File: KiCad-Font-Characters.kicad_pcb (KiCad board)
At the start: 2 copper layers, 453 x 498 mm, 0 parts

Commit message: Formatting (bold headers, bottom-line)
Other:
- board size 453 x 498 mm -> 453 x 501 mm
- board text added: "${COMPANY} - ${ISSUE_DATE}"
- board text added: "Arrows"
- board text added: "Basic Latin"
- board text added: "Currency Symbols"
- board text added: "Cyrillic Supplement"
- board text added: "General Punctuation"
- board text added: "Greek Extended"
- board text added: "Greek and Coptic"
- board text added: "Halfwidth and Fullwidth Forms"
- board text added: "IPA Extensions"
- board text added: "Latin Extended-B"
- board text added: "Latin1 Supplement"
- board text added: "Mathematical Operators"
- board text added: "Phonetic Extensions"
- board text added: "Superscripts and Subscripts"

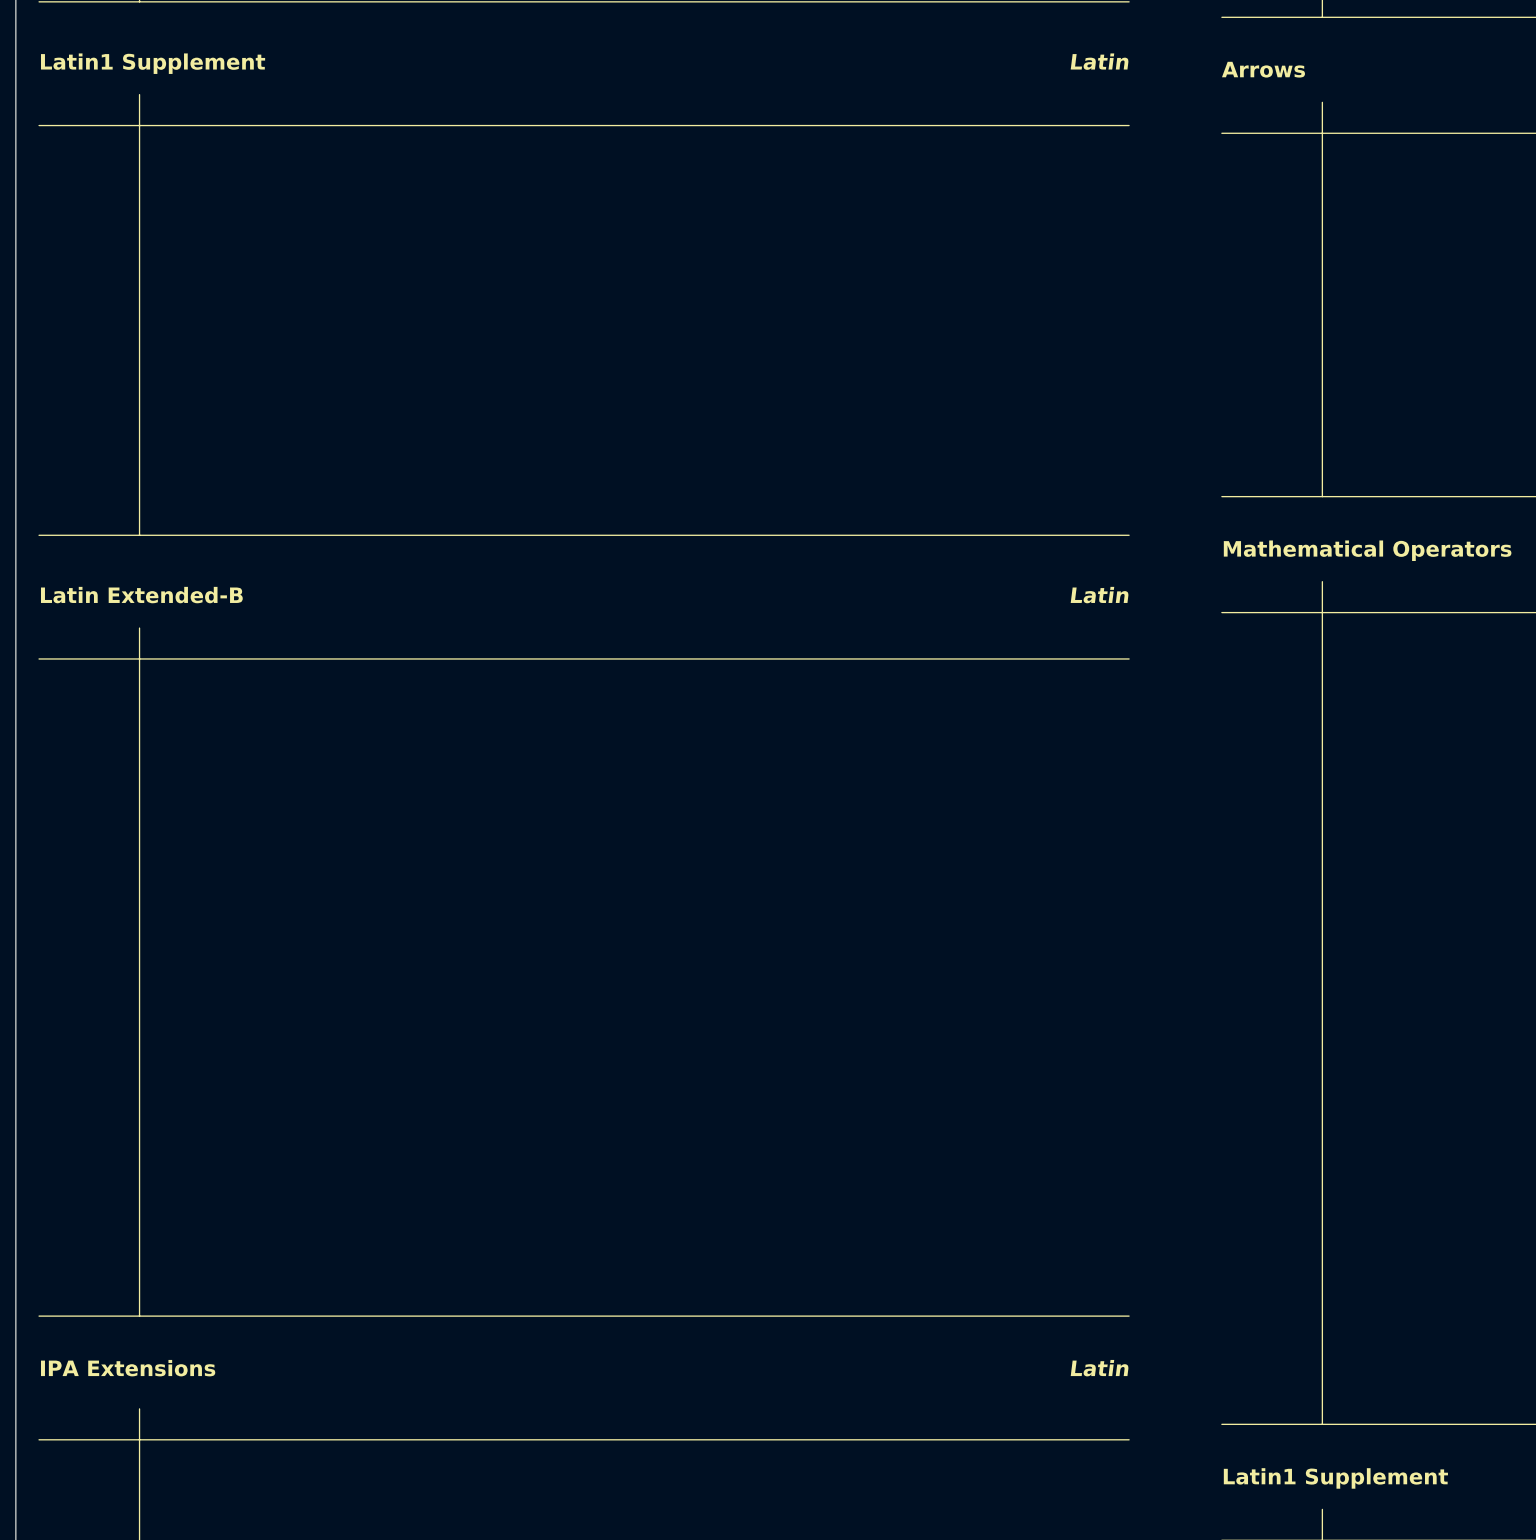
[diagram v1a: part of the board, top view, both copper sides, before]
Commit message: Fixed wrong block names
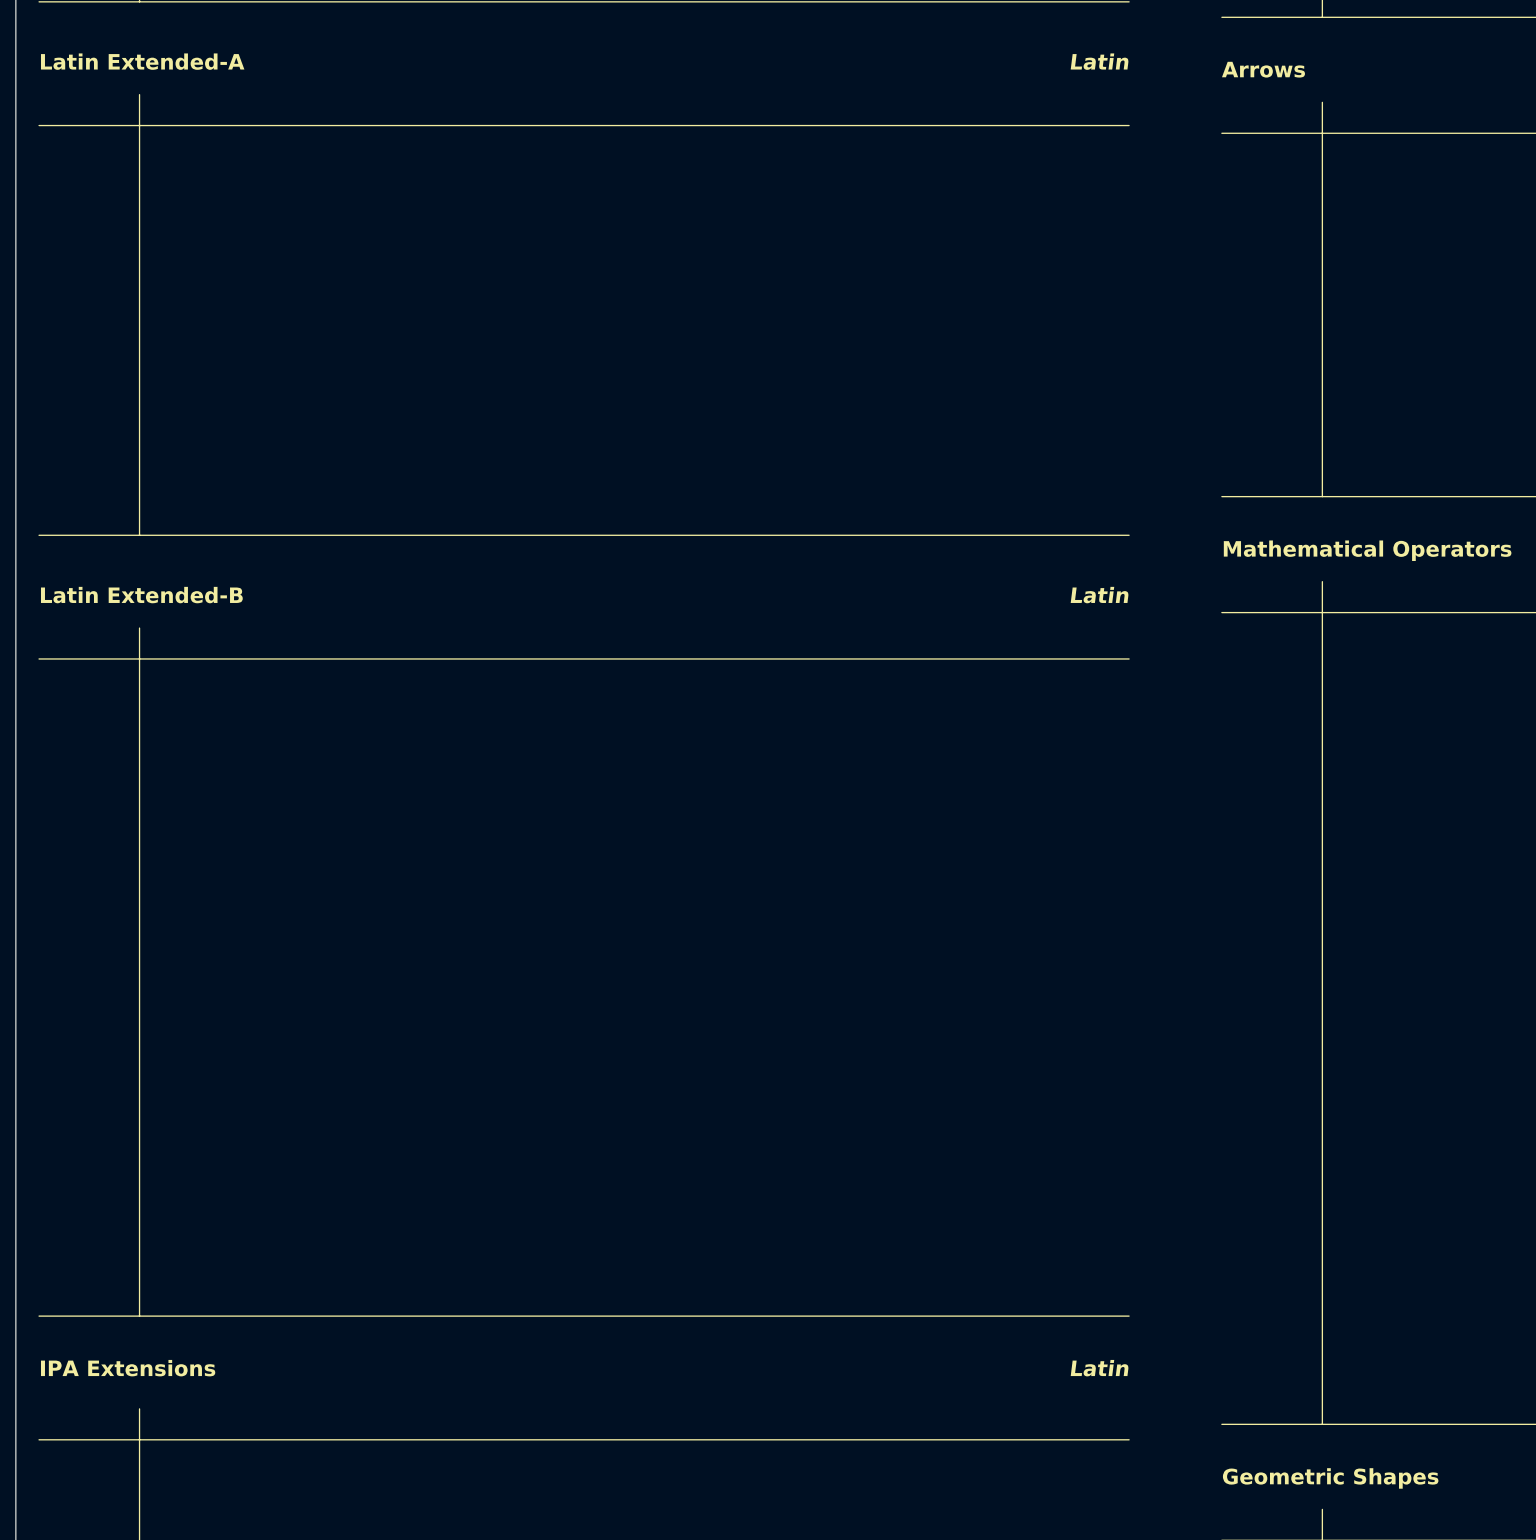
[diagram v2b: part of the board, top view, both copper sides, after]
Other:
- board text added: "Geometric Shapes"
- board text added: "Latin Extended-A"
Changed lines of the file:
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@@
       (sketchpadsonfab false)
       (subtractmaskfromsilk false)
-      (outputformat 5)
+      (outputformat 4)
       (mirror false)
       (drillshape 0)
@@
     (effects (font (size 2 2) (thickness 0.4) bold italic) (justify right bottom))
   )
-  (gr_text "Latin1 Supplement" (at 3 133) (layer "F.SilkS")
+  (gr_text "Latin Extended-A" (at 3 133) (layer "F.SilkS")
     (effects (font (size 2 2) (thickness 0.4) bold) (justify left bottom))
   )
@@
     (effects (font (size 2 2) (thickness 0.4) bold italic) (justify right bottom))
   )
-  (gr_text "Latin1 Supplement" (at 156 316) (layer "F.SilkS")
+  (gr_text "Geometric Shapes" (at 156 316) (layer "F.SilkS")
     (effects (font (size 2 2) (thickness 0.4) bold) (justify left bottom))
   )

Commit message: Fixed annotations
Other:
- board text added: "Grouped by Script. Unimplemented blocks are omitted. ${COMPANY} - ${ISSUE_DATE}"
- board text removed: "${COMPANY} - ${ISSUE_DATE}"
- board text removed: "Unimplemented Blocks are omitted Grouped by Writing System (Script)"
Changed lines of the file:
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@@
     (effects (font (size 2 2) (thickness 0.4) bold italic) (justify right bottom))
   )
-  (gr_text "${COMPANY} - ${ISSUE_DATE}" (at 450 499.117499) (layer "F.SilkS")
+  (gr_text "Grouped by Script.\n\nUnimplemented blocks are omitted.\n\n${COMPANY} - ${ISSUE_DATE}" (at 450 499.117499) (layer "F.SilkS")
     (effects (font (size 2 2) (thickness 0.3)) (justify right bottom))
-  )
-  (gr_text "Unimplemented Blocks are omitted\nGrouped by Writing System (Script)" (at 450 2) (layer "F.SilkS")
-    (effects (font (size 3 3) (thickness 0.375) italic) (justify right top))
   )
   (gr_text "Latin Extended-B" (at 3 202) (layer "F.SilkS")
@@
   (group "" (id 77080d20-7dbb-40e9-8009-72fe85131f03)
     (members
-      2d7b8c22-9c47-4364-9aad-18bd9f6cd68d
       5534f6d2-ff0e-4ebf-ba5c-00a53f904439
       5773e85d-3e22-4831-99a1-efc79fa955a9
